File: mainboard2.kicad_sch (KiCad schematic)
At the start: 33 parts, among them J1 Conn_01x03_Socket, J10 Conn_01x03_Socket, J11 Conn_01x02_Socket, J12 Conn_01x02_Socket, J13 Conn_01x04_Socket, J2 Conn_01x03_Socket, J3 GPIO, J4 Conn_01x03_Socket, J5 Conn_01x03_Socket, J6 Conn_01x03_Socket, J7 Conn_01x03_Socket, J8 Conn_01x02_Socket, J9 Conn_01x03_Socket, Q5 IRFML8244TRPBF, U1 PCA9685PW, U2 PCA9685PW, U3 MCP3208

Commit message: コンデンサを追加
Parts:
- renumbered C3 to C1, C4 to C41, C2 to C42, C1 to C46, J12 to J11, J3 to J12, J11 to J13, J6 to J14, J7 to J15, J4 to J16, J5 to J17, J1 to J18, J2 to J19, J8 to J2, J13 to J20, R60 to R25, R59 to R26, R5 to R30, R3 to R31, R4 to R32, R1 to R34, R2 to R35, R8 to R36, R6 to R37, R7 to R38, U3 to U4, U2 to U5, U1 to U7

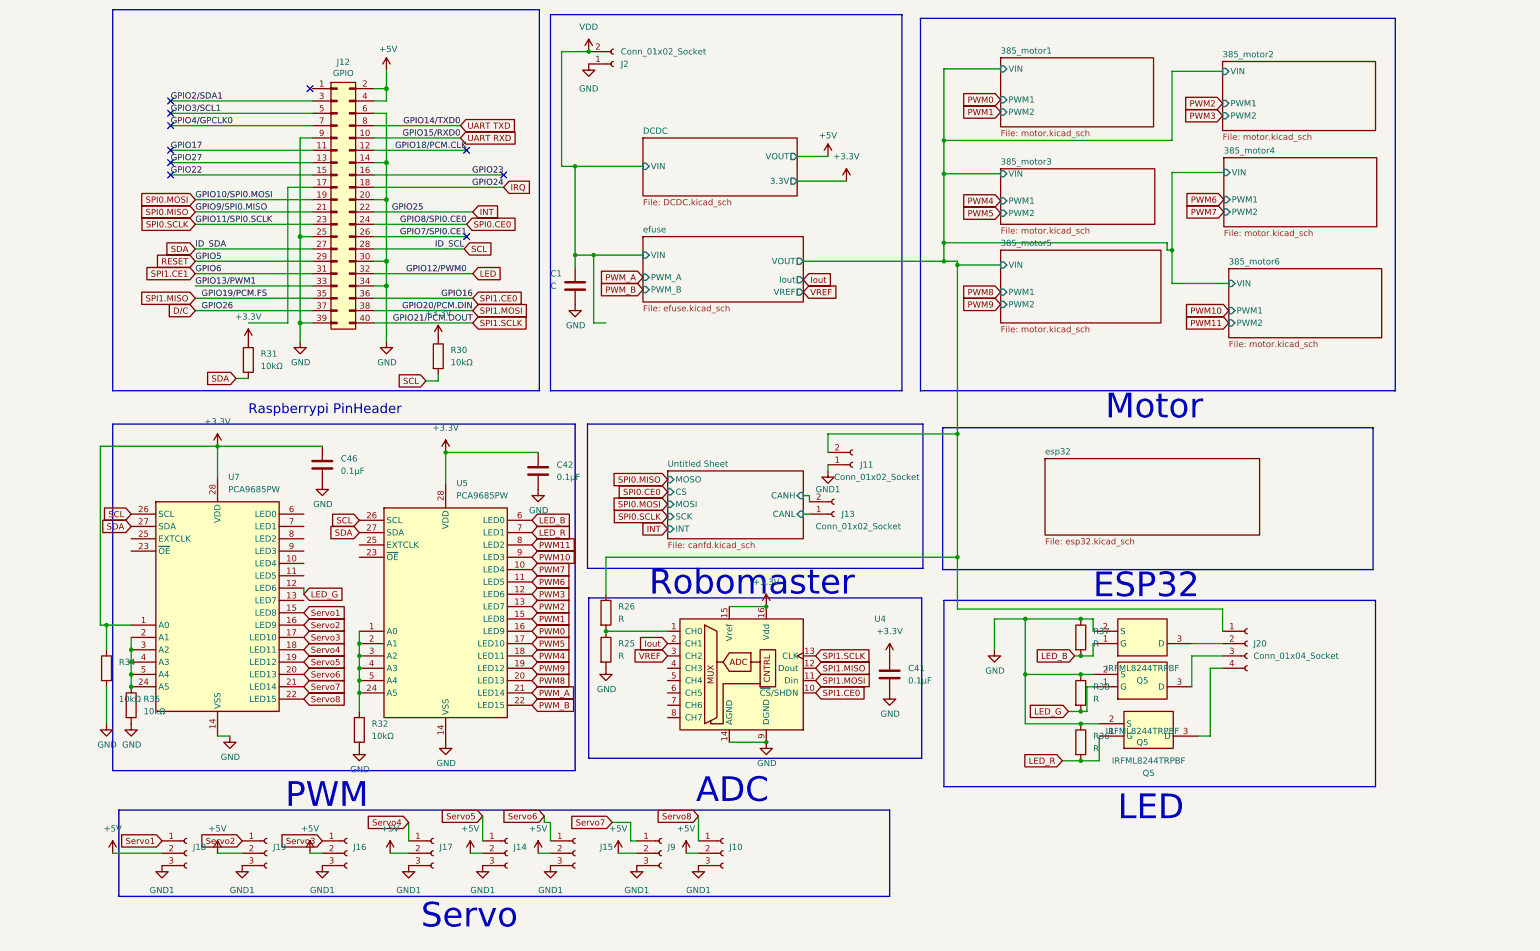
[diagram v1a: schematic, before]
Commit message: 電流センサー変更
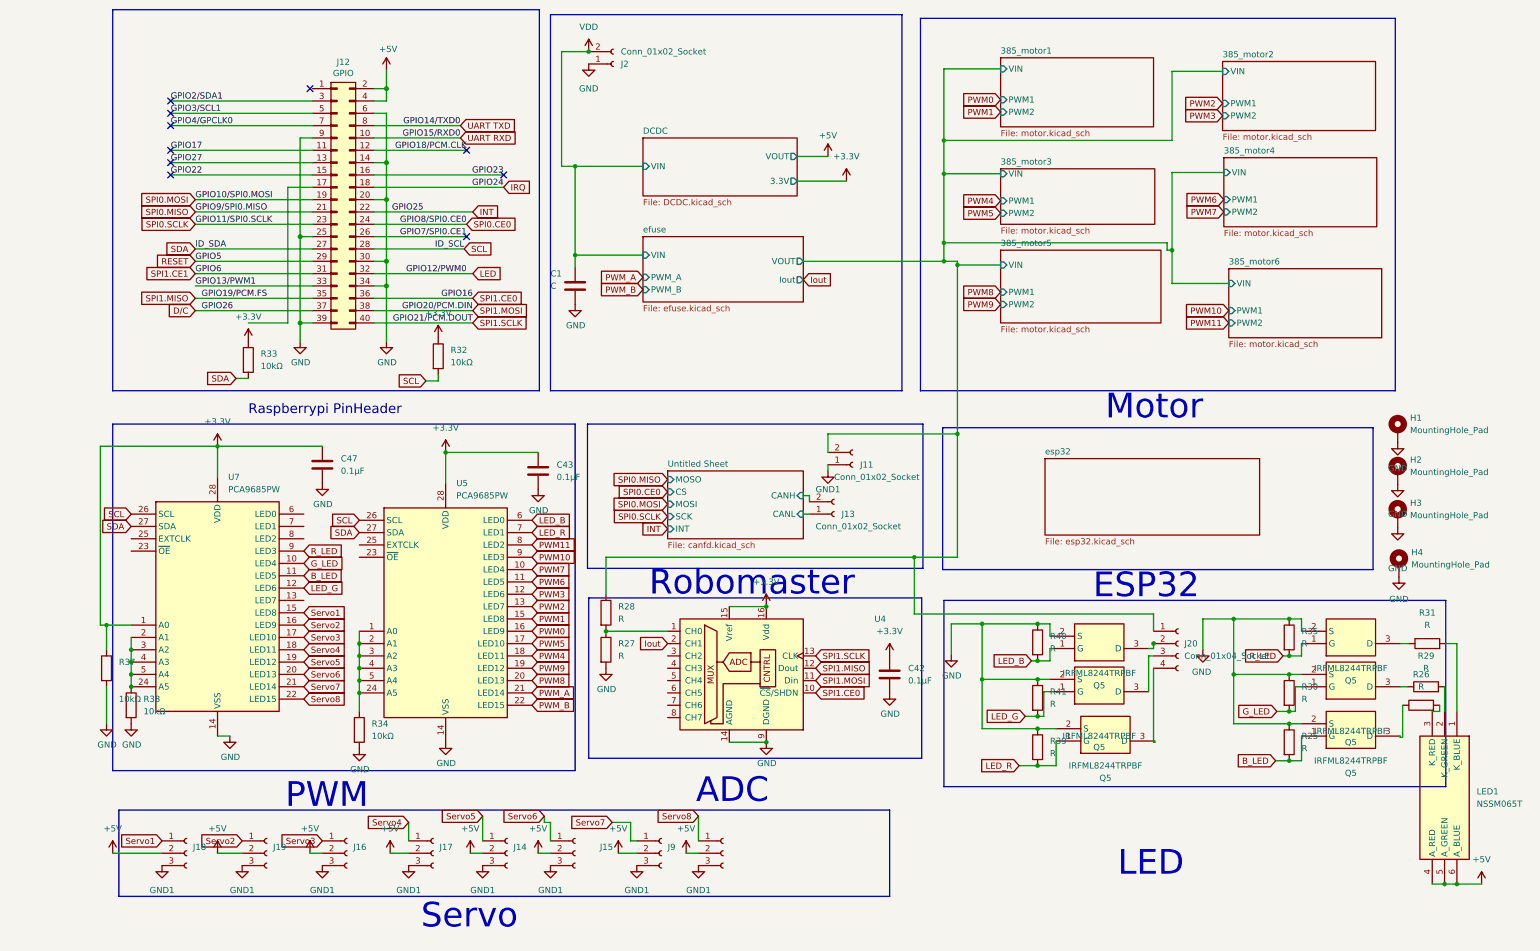
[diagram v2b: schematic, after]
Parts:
- added H1, H2, H3, H4: MountingHole_Pad, MountingHole:MountingHole_3.2mm_M3_DIN965_Pad, symbol Mechanical:MountingHole_Pad
- added LED1: NSSM065T, Library:NSSM065T, symbol NSSM065T:NSSM065T
- added Q5 (x3): IRFML8244TRPBF, Package_TO_SOT_SMD:SOT-23-3, symbol SamacSys_Parts:IRFML8244TRPBF
- added R25, R26, R29, R30, R31, R35: R, Resistor_SMD:R_0603_1608Metric_Pad0.98x0.95mm_HandSolder, symbol Device:R
- J13: footprint Connector_JST:JST_XH_S2B-XH-A-1_1x02_P2.50mm_Horizontal -> Connector_JST:JST_XH_B2B-XH-A_1x02_P2.50mm_Vertical
- renumbered C41 to C42, C42 to C43, C46 to C47, R25 to R27, R26 to R28, R30 to R32, R31 to R33, R32 to R34, R34 to R37, R35 to R38, R36 to R39, R37 to R40, R38 to R41
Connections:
- net +5V: now also LED1.4 (A_RED), LED1.5 (A_GREEN), LED1.6 (A_BLUE)
- net GND: now also H1.1, H2.1, H3.1, H4.1, Q5.2 (S), Q5.2 (S), Q5.2 (S), R25.1, R30.1, R35.1
- net G_LED: now reaches U7.10 (LED4)
- net G_LED: now also Q5.1 (G), R30.2
- net B_LED: now reaches U7.11 (LED5)
- net B_LED: now also Q5.1 (G), R25.2
- net R_LED: now reaches U7.9 (LED3)
- net R_LED: now also Q5.1 (G), R35.2
- net VREF: no longer names the net of U4.3 (CH2)
- new net: Q5.3 (D), R31.1
- new net: Q5.3 (D), R29.1
- new net: LED1.2 (K_GREEN), R29.2
- new net: Q5.3 (D), R26.1
- new net: LED1.3 (K_RED), R26.2
- new net: LED1.1 (K_BLUE), R31.2
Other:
- sheet efuse ports: added none; removed VREF
- moved on the sheet: J20, Q5, R39, R40, R41

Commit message: ESP32バージョン
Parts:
- removed C42, C47: 0.1μF, Capacitor_SMD:C_0603_1608Metric_Pad1.08x0.95mm_HandSolder, symbol Device:C
- removed J11: Conn_01x02_Socket, Connector_AMASS:AMASS_XT30PW-M_1x02_P2.50mm_Horizontal, symbol Connector:Conn_01x02_Socket
- removed J12: GPIO, Connector_PinSocket_2.54mm:PinSocket_2x20_P2.54mm_Vertical, symbol Connector_Generic:Conn_02x20_Odd_Even
- removed R32, R33, R37, R38: 10kΩ, Resistor_SMD:R_0603_1608Metric_Pad0.98x0.95mm_HandSolder, symbol Device:R
- removed U4: MCP3208, Library:SOIC127P600X175-16N, symbol Analog_ADC:MCP3208
- removed U7: PCA9685PW, Package_SO:TSSOP-28_4.4x9.7mm_P0.65mm, symbol Driver_LED:PCA9685PW
- added C17: 0.1u, Capacitor_SMD:C_0603_1608Metric_Pad1.08x0.95mm_HandSolder, symbol Device:C
- added J12: Conn_01x02_Socket, Connector_JST:JST_XH_B2B-XH-A_1x02_P2.50mm_Vertical, symbol Connector:Conn_01x02_Socket
- added J13: USB_C_Receptacle_USB2.0, Connector_USB:USB_C_Receptacle_HCTL_HC-TYPE-C-16P-01A, symbol Connector:USB_C_Receptacle_USB2.0
- added R28: 5.1k, Resistor_SMD:R_0603_1608Metric_Pad0.98x0.95mm_HandSolder, symbol Device:R
- added R5: 10kΩ, Resistor_SMD:R_0603_1608Metric_Pad0.98x0.95mm_HandSolder, symbol Device:R
- added SW2: SW_Push_Dual_x2, Button_Switch_SMD:SW_Push_1P1T_NO_CK_KMR2, symbol Switch:SW_Push_Dual_x2
- added U3: ESP32-WROOM-E, PCM_Espressif:ESP32-WROOM-32E, symbol PCM_Espressif:ESP32-WROOM-E
- added U4: MCP2562-E-SN, Package_SO:SOIC-8_3.9x4.9mm_P1.27mm, symbol Interface_CAN_LIN:MCP2562-E-SN
- added U6: CH330N, Package_SO:SOIC-8_3.9x4.9mm_P1.27mm, symbol Interface_USB:CH330N
- J13: footprint Connector_JST:JST_XH_B2B-XH-A_1x02_P2.50mm_Vertical -> Connector_AMASS:AMASS_XT30PW-F_1x02_P2.50mm_Horizontal
- J20: footprint Connector_JST:JST_XH_S4B-XH-A_1x04_P2.50mm_Horizontal -> Connector_JST:JST_XH_B4B-XH-A_1x04_P2.50mm_Vertical
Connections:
- net Untitled Sheet/CANL is gone; now on net GND1: J13.1 (Pin_1)
- net +3.3V: now also R5.1, U3.2 (3V3), U4.5 (Vio)
- net +5V: now also J13.A4 (VBUS), J13.A9 (VBUS), J13.B4 (VBUS), J13.B9 (VBUS), U4.3 (VDD)
- net B_LED: now also U3.12 (ADC2_CH7/GPIO27)
- net GND: now also SW2.1 (C)
- net R_LED: now also U3.10 (DAC_1/ADC2_CH8/GPIO25)
- net Servo1: now also U3.11 (DAC_2/ADC2_CH9/GPIO26)
- net Servo2: now also U3.24 (ADC2_CH2/GPIO2)
- net Servo3: now also U3.26 (ADC2_CH0/GPIO4)
- net Servo4: now also U3.29 (GPIO5)
- net Servo5: now also U3.27 (GPIO16)
- net Servo6: now also U3.28 (GPIO17)
- net Servo7: now also U3.30 (GPIO18)
- net Servo8: now also U3.36 (GPIO22)
- net Untitled Sheet/CANH: no longer names the net of J13.2 (Pin_2)
- new net: U3.1 (GND), U3.15 (GND), U3.38 (GND)
- new net: R5.2, SW2.2 (D), U3.3 (EN/CHIP_PU)
- new net: J13.B5 (CC2), R28.1
- new net: J12.2 (Pin_2), U4.6 (CANL)
- new net: J12.1 (Pin_1), U4.7 (CANH)
- new net: J13.A6 (D+), J13.B6 (D+), U6.1 (UD+)
- new net: J13.A7 (D-), J13.B7 (D-), U6.2 (UD-)
- new net CANRX: U4.4 (RXD)
- new net CANTX: U4.1 (TXD)
- new net GNDA: C17.1, J13.A1 (GND), J13.A12 (GND), J13.B1 (GND), J13.B12 (GND), J13.S1 (SHIELD), R28.2, U4.2 (VSS), U4.8 (STBY), U6.3 (GND)
- new net RXCAN: U3.25 (GPIO0/BOOT/ADC2_CH1)
- new net TXCAN: U3.33 (GPIO21)
- new net UART_RX: U3.35 (U0TXD/GPIO1), U6.7 (RXD)
- new net UART_TX: U3.34 (U0RXD/GPIO3), U6.6 (TXD)
- no-connect marks 10 -> 0
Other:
- removed sheet Untitled Sheet
- note removed: "ADC"
- note removed: "ESP32"
- note removed: "Robomaster"
- moved on the sheet: C43, H1, H2, H3, H4, R27, R28, R34, U5
